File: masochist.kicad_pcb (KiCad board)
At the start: 2 copper layers, 195.3 x 103.2 mm, 76 parts, among them J1 USB_C_Receptacle_USB2.0, J2 AVR-ISP-6, SW1 RESET, SW2 SW_Push, U1 ATmega328P-PU, Y1 Crystal

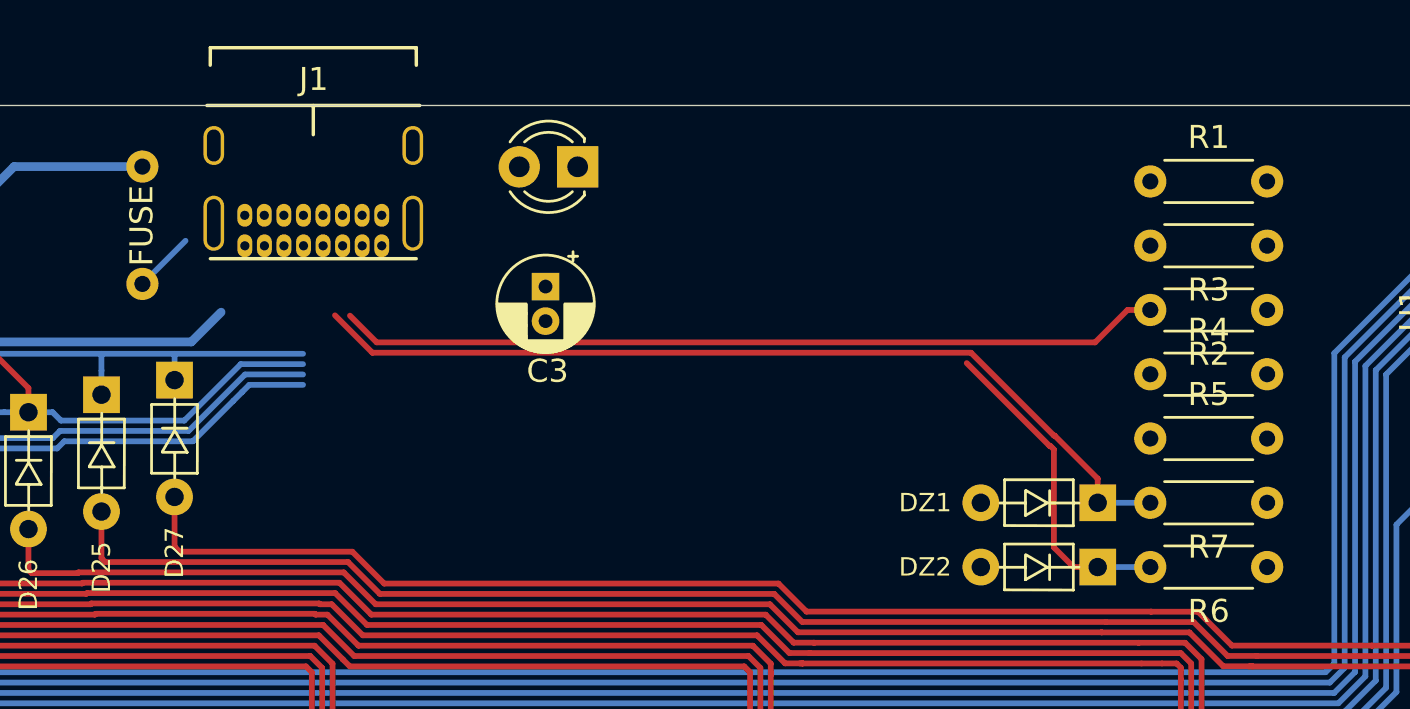
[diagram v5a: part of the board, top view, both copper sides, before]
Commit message: Forgot to connect the BOOT switch to anything in the schematic
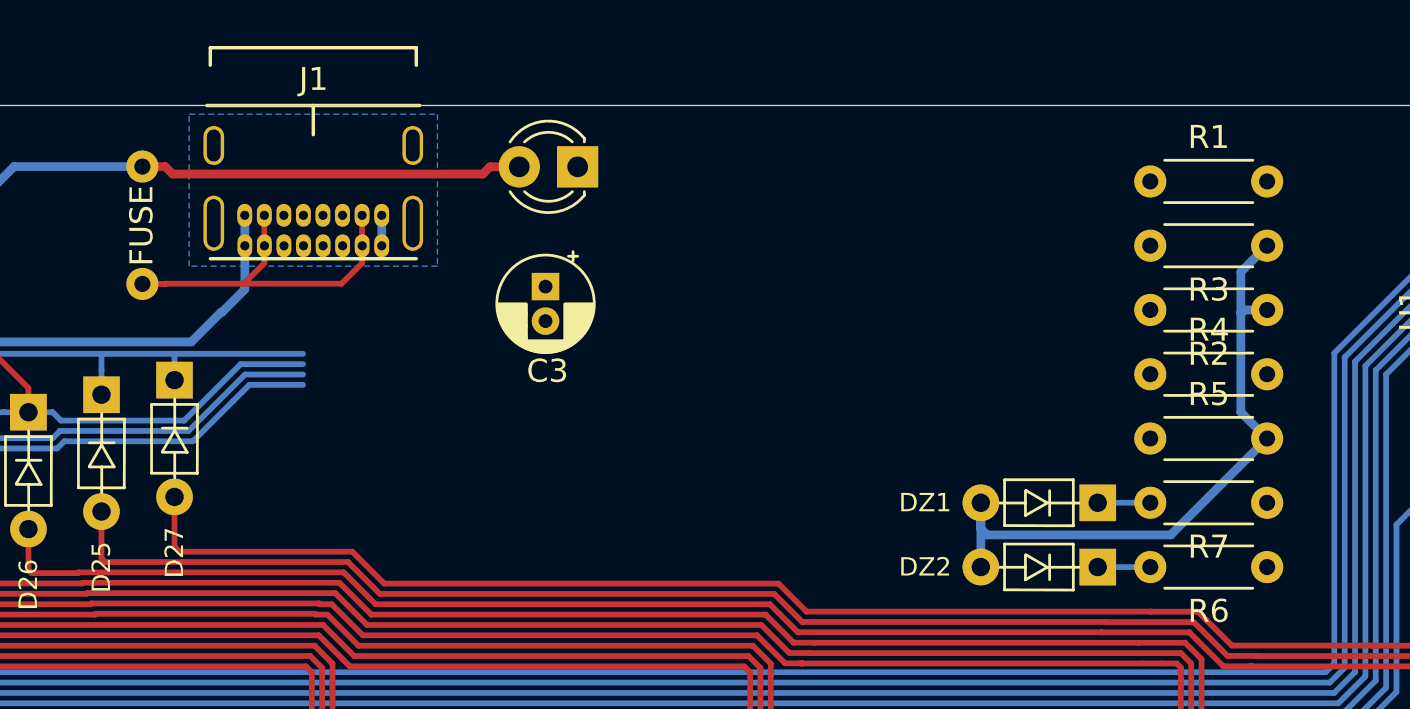
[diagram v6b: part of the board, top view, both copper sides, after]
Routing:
- net Net-(DZ1-Pad1): track 39.4 -> 2.29 mm
- net Net-(J1-PadA5): track 35.9 -> 0.00 mm
- net GND: track 53.4 -> 88.1 mm
- net +5V: track 16.0 -> 32.6 mm
- net Net-(F1-Pad2): track 2.65 -> 15.4 mm
- net Net-(DZ2-Pad1): track 14.1 -> 2.29 mm
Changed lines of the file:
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@@
     (thickness 1.6)
     (drawings 32)
-    (tracks 680)
+    (tracks 699)
     (zones 0)
     (modules 76)
@@
   (segment (start 136.034213 39.243) (end 140.589 39.243) (width 0.38) (layer F.Cu) (net 1))
   (segment (start 134.62 39.243) (end 136.034213 39.243) (width 0.38) (layer F.Cu) (net 1))
-  (segment (start 140.589 39.243) (end 140.716 39.243) (width 0.38) (layer B.Cu) (net 1))
-  (segment (start 140.716 39.243) (end 143.50299 42.02999) (width 0.38) (layer B.Cu) (net 1))
-  (segment (start 158.21101 42.02999) (end 159.505 40.736) (width 0.38) (layer B.Cu) (net 1))
-  (segment (start 143.50299 42.02999) (end 158.21101 42.02999) (width 0.38) (layer B.Cu) (net 1))
   (segment (start 228.934 36.71825) (end 228.82225 36.83) (width 0.38) (layer B.Cu) (net 1))
   (segment (start 228.934 34.163) (end 228.934 36.71825) (width 0.38) (layer B.Cu) (net 1))
@@
   (segment (start 225.552 52.498) (end 226.68337 52.498) (width 0.38) (layer B.Cu) (net 1))
   (segment (start 226.68337 52.498) (end 228.139 52.498) (width 0.38) (layer B.Cu) (net 1))
+  (segment (start 160.5375 36.53) (end 160.5325 36.525) (width 0.38) (layer B.Cu) (net 1))
+  (segment (start 160.5375 37.85) (end 160.5375 36.53) (width 0.38) (layer B.Cu) (net 1))
+  (segment (start 166.4875 37.85) (end 166.4875 36.525) (width 0.38) (layer B.Cu) (net 1))
+  (segment (start 160.5375 39.7415) (end 160.5375 37.85) (width 0.38) (layer B.Cu) (net 1))
+  (segment (start 140.716 39.243) (end 143.50299 42.02999) (width 0.38) (layer B.Cu) (net 1))
+  (segment (start 140.589 39.243) (end 140.716 39.243) (width 0.38) (layer B.Cu) (net 1))
+  (segment (start 159.543 40.736) (end 160.5375 39.7415) (width 0.38) (layer B.Cu) (net 1))
+  (segment (start 143.50299 42.02999) (end 158.21101 42.02999) (width 0.38) (layer B.Cu) (net 1))
+  (segment (start 158.21101 42.02999) (end 159.505 40.736) (width 0.38) (layer B.Cu) (net 1))
+  (segment (start 159.505 40.736) (end 159.543 40.736) (width 0.38) (layer B.Cu) (net 1))
+  (segment (start 192.532 49.022) (end 192.532 51.816) (width 0.38) (layer B.Cu) (net 1))
+  (segment (start 192.532 50.15337) (end 192.79763 50.419) (width 0.38) (layer B.Cu) (net 1))
+  (segment (start 192.532 49.022) (end 192.532 50.15337) (width 0.38) (layer B.Cu) (net 1))
+  (segment (start 200.787 50.419) (end 204.978 46.228) (width 0.38) (layer B.Cu) (net 1))
+  (segment (start 192.79763 50.419) (end 200.787 50.419) (width 0.38) (layer B.Cu) (net 1))
+  (segment (start 203.835 38.989) (end 204.978 37.846) (width 0.38) (layer B.Cu) (net 1))
+  (segment (start 204.978 46.228) (end 203.835 45.085) (width 0.38) (layer B.Cu) (net 1))
+  (segment (start 204.978 40.64) (end 203.988051 40.64) (width 0.38) (layer B.Cu) (net 1))
+  (segment (start 203.861051 40.767) (end 203.835 40.767) (width 0.38) (layer B.Cu) (net 1))
+  (segment (start 203.988051 40.64) (end 203.861051 40.767) (width 0.38) (layer B.Cu) (net 1))
+  (segment (start 203.835 45.085) (end 203.835 40.767) (width 0.38) (layer B.Cu) (net 1))
+  (segment (start 203.835 40.767) (end 203.835 38.989) (width 0.38) (layer B.Cu) (net 1))
   (segment (start 232.791 51.054) (end 233.934 49.911) (width 0.25) (layer B.Cu) (net 2))
   (segment (start 228.981 51.054) (end 232.791 51.054) (width 0.25) (layer B.Cu) (net 2))
@@
   (segment (start 228.82225 44.60875) (end 228.82225 44.45) (width 0.38) (layer B.Cu) (net 4))
   (segment (start 150.505 34.407) (end 156.083 34.407) (width 0.38) (layer B.Cu) (net 4))
+  (segment (start 171.193208 34.417) (end 172.466 34.417) (width 0.38) (layer F.Cu) (net 4))
+  (segment (start 157.395959 34.73001) (end 170.880198 34.73001) (width 0.38) (layer F.Cu) (net 4))
+  (segment (start 157.072949 34.407) (end 157.395959 34.73001) (width 0.38) (layer F.Cu) (net 4))
+  (segment (start 170.880198 34.73001) (end 171.193208 34.417) (width 0.38) (layer F.Cu) (net 4))
+  (segment (start 156.083 34.407) (end 157.072949 34.407) (width 0.38) (layer F.Cu) (net 4))
   (segment (start 73.66 56.388) (end 73.66 63.02375) (width 0.25) (layer F.Cu) (net 5))
   (segment (start 73.66 63.02375) (end 73.9775 63.34125) (width 0.25) (layer F.Cu) (net 5))
@@
   (segment (start 201.972999 53.756954) (end 203.445799 55.229754) (width 0.25) (layer F.Cu) (net 35))
   (segment (start 197.612 49.022) (end 199.898 49.022) (width 0.25) (layer B.Cu) (net 36))
-  (segment (start 197.612 49.022) (end 197.612 47.972) (width 0.25) (layer F.Cu) (net 36))
-  (segment (start 197.612 47.972) (end 195.741 46.101) (width 0.25) (layer F.Cu) (net 36))
-  (segment (start 166.0816 42.49901) (end 164.45499 40.8724) (width 0.25) (layer F.Cu) (net 36))
-  (segment (start 192.105011 42.499011) (end 166.0816 42.49901) (width 0.25) (layer F.Cu) (net 36))
-  (segment (start 195.741 46.101) (end 195.707 46.101) (width 0.25) (layer F.Cu) (net 36))
-  (segment (start 195.707 46.101) (end 192.105011 42.499011) (width 0.25) (layer F.Cu) (net 36))
   (segment (start 197.612 51.816) (end 199.898 51.816) (width 0.25) (layer B.Cu) (net 37))
-  (segment (start 195.707 50.961) (end 195.707 46.70341) (width 0.25) (layer F.Cu) (net 37))
-  (segment (start 197.612 51.816) (end 196.562 51.816) (width 0.25) (layer F.Cu) (net 37))
-  (segment (start 196.562 51.816) (end 195.707 50.961) (width 0.25) (layer F.Cu) (net 37))
-  (segment (start 195.520599 46.551009) (end 191.91861 42.94902) (width 0.25) (layer F.Cu) (net 37))
-  (segment (start 195.707 46.70341) (end 195.5546 46.55101) (width 0.25) (layer F.Cu) (net 37))
-  (segment (start 195.5546 46.55101) (end 195.520599 46.551009) (width 0.25) (layer F.Cu) (net 37))
-  (segment (start 156.083 39.507) (end 157.95901 37.63099) (width 0.25) (layer B.Cu) (net 38))
-  (segment (start 166.268001 42.049001) (end 165.105 40.886) (width 0.25) (layer F.Cu) (net 39))
-  (segment (start 198.908051 40.64) (end 197.49905 42.049001) (width 0.25) (layer F.Cu) (net 39))
-  (segment (start 197.49905 42.049001) (end 166.268001 42.049001) (width 0.25) (layer F.Cu) (net 39))
-  (segment (start 199.898 40.64) (end 198.908051 40.64) (width 0.25) (layer F.Cu) (net 39))
+  (segment (start 157.072949 39.507) (end 157.082949 39.497) (width 0.25) (layer F.Cu) (net 38))
+  (segment (start 156.083 39.507) (end 157.072949 39.507) (width 0.25) (layer F.Cu) (net 38))
+  (segment (start 161.3875 38.6) (end 161.3875 37.85) (width 0.25) (layer F.Cu) (net 38))
+  (segment (start 160.4905 39.497) (end 161.3875 38.6) (width 0.25) (layer F.Cu) (net 38))
+  (segment (start 161.3825 37.845) (end 161.3875 37.85) (width 0.25) (layer F.Cu) (net 38))
+  (segment (start 161.3825 36.525) (end 161.3825 37.845) (width 0.25) (layer F.Cu) (net 38))
+  (segment (start 165.6325 37.845) (end 165.6375 37.85) (width 0.25) (layer F.Cu) (net 38))
+  (segment (start 165.6325 36.525) (end 165.6325 37.845) (width 0.25) (layer F.Cu) (net 38))
+  (segment (start 164.7405 39.497) (end 160.528 39.497) (width 0.25) (layer F.Cu) (net 38))
+  (segment (start 165.6375 38.6) (end 164.7405 39.497) (width 0.25) (layer F.Cu) (net 38))
+  (segment (start 165.6375 37.85) (end 165.6375 38.6) (width 0.25) (layer F.Cu) (net 38))
+  (segment (start 157.082949 39.497) (end 160.528 39.497) (width 0.25) (layer F.Cu) (net 38))
+  (segment (start 160.528 39.497) (end 160.4905 39.497) (width 0.25) (layer F.Cu) (net 38))
   (segment (start 117.469213 34.743) (end 122.555 34.743) (width 0.25) (layer F.Cu) (net 44))
   (segment (start 116.055 34.743) (end 117.469213 34.743) (width 0.25) (layer F.Cu) (net 44))
@@
       )
     )
+  )
+  (zone (net 1) (net_name GND) (layer B.Cu) (hatch edge 0.508)
+    (connect_pads (clearance 0.508))
+    (min_thickness 0.254)
+    (fill yes (arc_segments 32) (thermal_gap 0.508) (thermal_bridge_width 0.508))
+    (polygon
+      (pts
+        (xy 168.91 38.735) (xy 158.115 38.735) (xy 158.115 32.131) (xy 168.91 32.131)
+      )
+    )

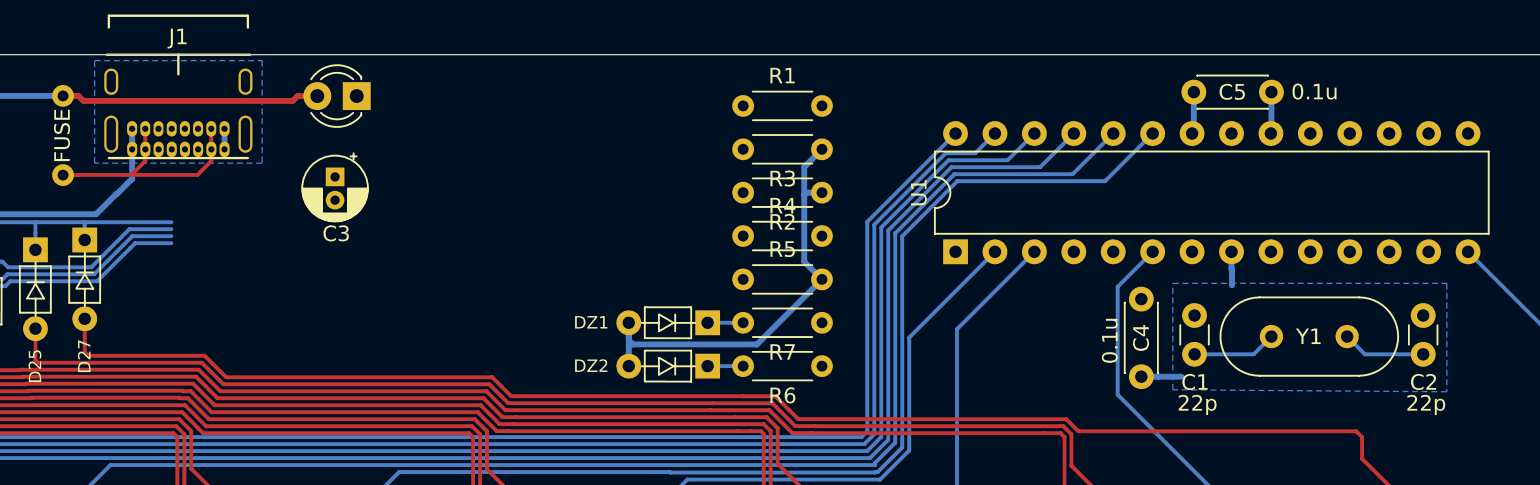
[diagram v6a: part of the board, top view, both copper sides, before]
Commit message: updated pin assignments to make routing easier
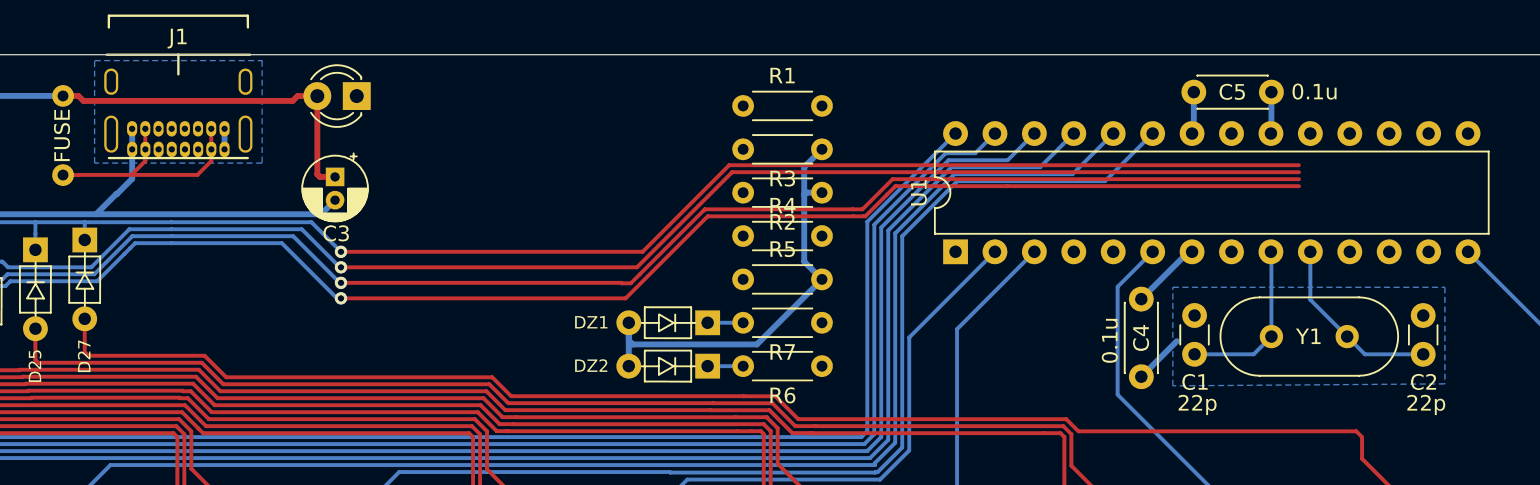
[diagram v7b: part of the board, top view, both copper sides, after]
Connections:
- U1 pad 11: Net-(U1-Pad11) -> BOOT
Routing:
- net ROW2: track 114.2 -> 191.3 mm, vias 0 -> 1
- net ROW3: track 23.7 -> 100.4 mm, vias 0 -> 1
- net ROW1: track 113.5 -> 189.7 mm, vias 0 -> 1
- net ROW0: track 99.1 -> 174.9 mm, vias 0 -> 1
- net GND: track 88.1 -> 102.4 mm
- net +5V: track 32.6 -> 43.4 mm
- net XTAL2: track 5.37 -> 11.8 mm
- net XTAL1: track 5.47 -> 10.9 mm

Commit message: Traces Complete!
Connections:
- U1 pad 15: ROW0 -> ROW2
- U1 pad 16: ROW1 -> ROW3
- U1 pad 18: ROW3 -> ROW0
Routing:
- net BOOT: track 6.50 -> 123.5 mm, vias 0 -> 2
- net SCK: track 0.00 -> 115.7 mm, vias 0 -> 2
- net RESET: track 25.3 -> 124.0 mm, vias 0 -> 3
- net +5V: track 43.4 -> 129.9 mm, vias 0 -> 2
- net GND: track 102.4 -> 166.5 mm, vias 0 -> 1
- net Net-(DZ2-Pad1): track 2.29 -> 50.9 mm, vias 0 -> 1
- net Net-(DZ1-Pad1): track 2.29 -> 49.7 mm, vias 0 -> 1
- net Net-(J1-PadB5): track 0.00 -> 39.6 mm, vias 0 -> 2
- net Net-(J1-PadA5): track 0.00 -> 38.1 mm, vias 0 -> 1
- net Net-(LED1-Pad1): track 0.00 -> 34.8 mm
- net D-: track 0.00 -> 21.8 mm
- net D+: track 0.00 -> 18.1 mm
- net ROW2: track 191.3 -> 203.6 mm
- net ROW3: track 100.4 -> 109.9 mm
- net ROW1: track 189.7 -> 197.6 mm
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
